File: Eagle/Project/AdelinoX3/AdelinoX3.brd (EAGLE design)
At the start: 47.5 x 53.3 mm, 102 parts, among them J1 DC-044-A, J2 YELLOW-8P-2.54, J3 YELLOW-6P-2.54, J4 YELLOW-8P-2.54, J5 YELLOW-8P-2.54, J6 4P-2.0, J7 YELLOW-2X3P-2.54, J8 4P-2.0, Q1 NCE3407A, Q2 CJ2305, SW1 TS-1101F, U1 CJT1117-3.3, U2 MP1496DJ-SOT23-8, U3 ESP-12F / OPL: 317060163 / SM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, U4 DNP, U5 ATMEGA32U4-MUR-QFN44, U6 DNP, X1 306010049_XTAL_16MHZ-3225_4P

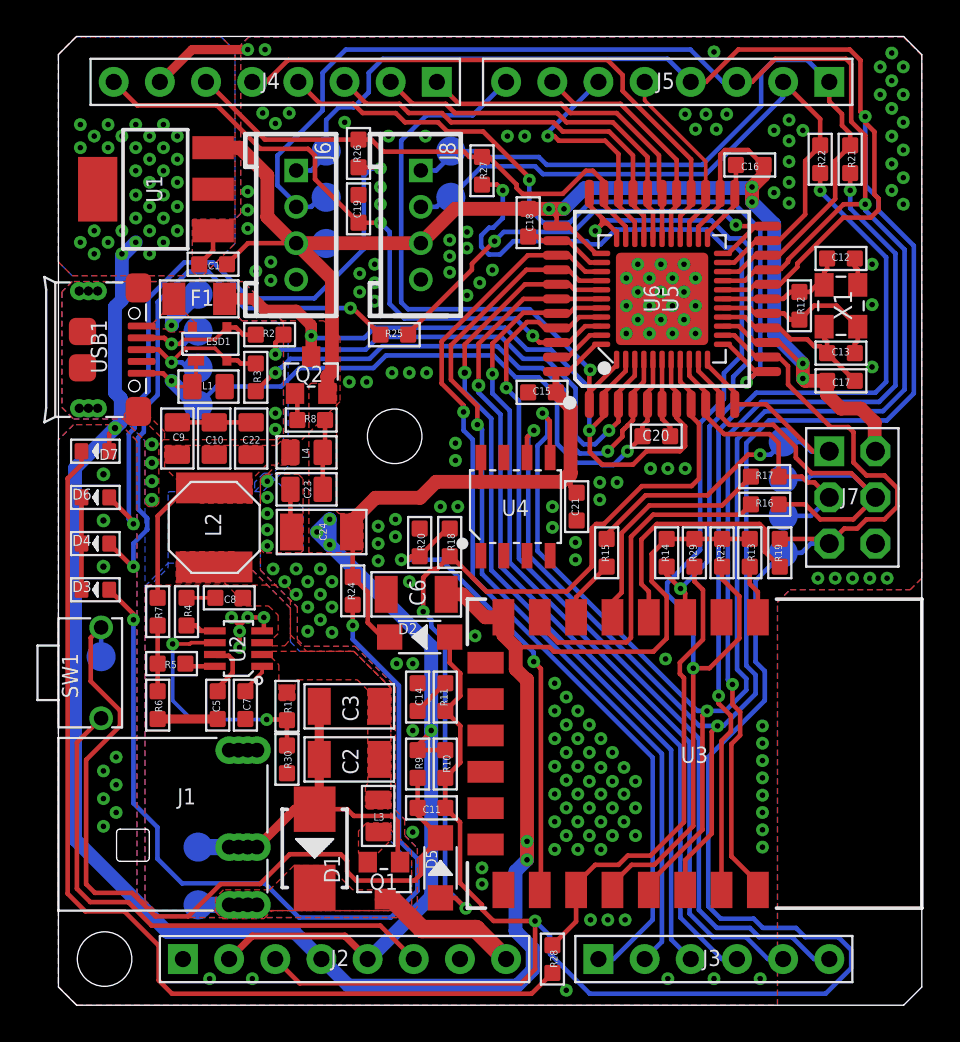
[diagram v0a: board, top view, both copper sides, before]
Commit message: Parts renumbered; tidy up silkscreen.
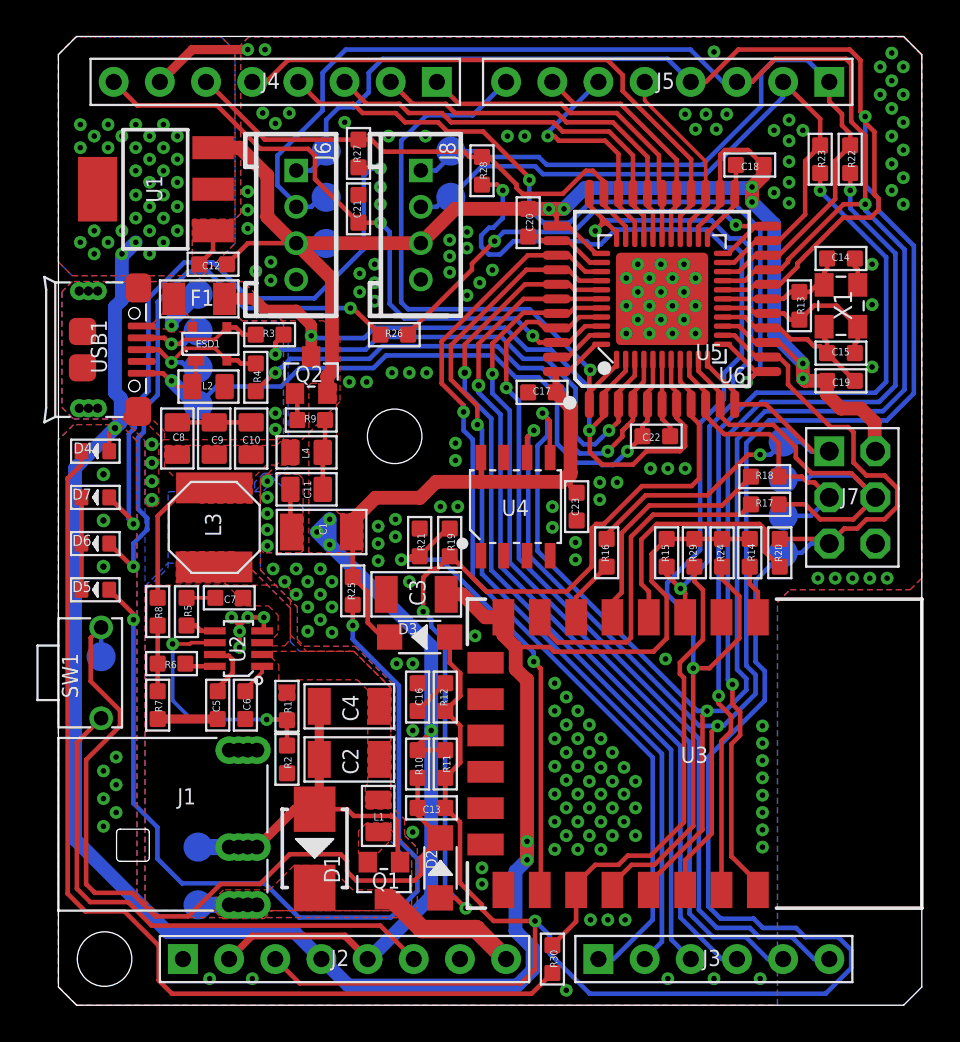
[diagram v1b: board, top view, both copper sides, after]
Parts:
- removed C24: 22uf, Seeed-Capacitor:C1206
- added C4: 22uf, Seeed-Capacitor:C1206
- C1: value 100nf -> 22uf; device OPL_Capacitor:C0603 -> Seeed-Capacitor:C1206
- C11, C8: value 100nf -> 10uf; device OPL_Capacitor:C0603 -> Seeed-Capacitor:C0805
- C12, C13: value 22pf -> 100nf; device Seeed-Capacitor:C0603 -> OPL_Capacitor:C0603
- C14, C15: value 100nf -> 22pf; device OPL_Capacitor:C0603 -> Seeed-Capacitor:C0603
- C20: value 1uf -> 100nf; device Seeed-Capacitor:C0603 -> OPL_Capacitor:C0603
- C21: device Seeed-Capacitor:C0603 -> OPL_Capacitor:C0603
- C22: value 10uf -> 1uf; device Seeed-Capacitor:C0805 -> Seeed-Capacitor:C0603
- C23: value 10uf -> 100nf; device Seeed-Capacitor:C0805 -> Seeed-Capacitor:C0603
- C3: device Seeed-Capacitor:C1206 -> OPL_Capacitor:C1206
- C6: value 22uf -> 22nf; device OPL_Capacitor:C1206 -> Seeed-Capacitor:C0603
- C7: value 22nf -> 100nf; device Seeed-Capacitor:C0603 -> OPL_Capacitor:C0603
- D3: value GRE-0603 -> 20V-500MA; device Seeed-LED:LED-0603 -> Seeed-Diode:SOD-123
- D4: value YEL-0603 -> BLU-0603
- D5: value 20V-500MA -> GRE-0603; device Seeed-Diode:SOD-123 -> Seeed-LED:LED-0603
- D7: value BLU-0603 -> YEL-0603
- L1: value 330R-1500MA -> 470R-2A; device Seeed-Inductor:L0805 -> OPL_Ferrite_and_Magnetic_Bead:L0805
- L2: value 10UH-225MA -> 330R-1500MA; device Seeed-Inductor:L5040S -> Seeed-Inductor:L0805
- L3: value 470R-2A -> 10UH-225MA; device OPL_Ferrite_and_Magnetic_Bead:L0805 -> Seeed-Inductor:L5040S
- R11: value 10K -> 100K
- R12: value 1M -> 10K
- R13: value 10K -> 1M
- R15, R24: value 1K -> 10K
- R19: value 0R -> 1K
- R2: value 22R -> 24K
- R20: value 100K -> 0R
- R21: value 1K -> 100K
- R23: value 10K -> 1K
- R28: value 470R -> 1K
- R30: value 24K -> 470R
- R4: value 10R -> 22R
- R5: value 3.3K -> 10R
- R6: value 3K / 1% -> 3.3K
- R7: value 2K7 / 1% -> 3K / 1%
- R8: value 100K -> 2K7 / 1%
- moved R28 43.5 mm to (23.3, 45.9), turned to 0 degrees
- moved C12 34.5 mm to (8.51, 40.8), turned to 90 degrees
- moved C16 34.5 mm to (19.8, 17.0), turned to 180 degrees
- moved C13 33.7 mm to (20.5, 10.9), turned to 270 degrees
- moved C14 33.5 mm to (43.1, 41.1), turned to 270 degrees
- moved R21 31.7 mm to (19.9, 25.5), turned to 0 degrees
- moved R12 29.0 mm to (21.3, 17.0)
- moved C19 28.2 mm to (43.1, 34.4), turned to 90 degrees
- moved L1 25.4 mm to (17.6, 10.4), turned to 90 degrees
- moved D5 24.4 mm to (2.03, 22.9), turned to 180 degrees
- moved R2 23.4 mm to (12.6, 13.5), turned to 180 degrees
- moved R23 22.3 mm to (41.9, 46.5)
- moved C22 22.3 mm to (32.9, 31.3), turned to 90 degrees
- moved R24 20.4 mm to (36.5, 24.9), turned to 180 degrees
- moved C21 20.3 mm to (16.5, 43.8), turned to 180 degrees
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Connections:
- net +3V3: now also C3.2, D4.+, R15.1, R24.2; no longer C6.2, D7.+, R13.1, R23.2
- net +5V: now also C11.2, C12.2, C19.1, C20.1, C23.1, D3.-, R10.1, R11.2, R25.1; no longer C15.1, C16.1, C21.1, C23.2, C24.2, D2.-, R10.2, R24.1, R8.1
- net ACT_LED: now also R26.1; no longer R25.1
- net AT_MISO: now also R16.1; no longer R15.1
- net AT_MOSI: now also R17.1; no longer R16.1
- net AT_SCK: now also R18.1; no longer R17.1
- net AT_SS: now also D2.+, R19.1; no longer D5.+, R18.1
- net BOOT_MODE: now also R24.1, R28.2; no longer R23.1, R27.2
- net D+: now also R4.2; no longer R3.2
- net D-: now also R3.2; no longer R2.2
- net ESP_EN: now also R15.2; no longer R14.2
- net GND: now also C11.1, C14.1, C15.1, C20.2, C23.2, C4.1, C8.1, D5.-, D7.-, L2.1, R2.1, R21.1, R7.1; no longer C13.1, C14.2, C15.2, C22.1, C23.1, C24.1, C7.1, D3.-, D4.-, L1.1, R20.1, R30.1, R6.1
- net GPIO12: now also R16.2; no longer R15.2
- net GPIO13: now also R17.2; no longer R16.2
- net GPIO14: now also R18.2; no longer R17.2
- net GPIO15: now also R19.2, R21.2; no longer R18.2, R20.2
- net GPIO16: now also R20.2; no longer R19.2
- net GPIO2_LED: now also R30.2; no longer R28.2
- net N$13: now also C16.1, R12.2; no longer C14.1, R11.2
- net N$15: now also C7.2, R5.2; no longer C8.2, R4.2
- net N$23: now also R7.2, R8.1; no longer R5.2, R7.1
- net N$3: now also R9.2; no longer R8.2
- net N$7: now also R2.2; no longer R30.2
- net N$8: now also L1.1; no longer L3.1
- net PIN_AREF: now also C21.1; no longer C19.1
- net PIN_D0: now also R22.2; no longer R21.2
- net PIN_D1: now also R23.2; no longer R22.2
- net PIN_D13: now also R28.1; no longer R26.1
- net RESET: now also C13.1, D3.+, R12.1, R20.1; no longer C11.1, D2.+, R10.1, R19.1
- net RST: now also R14.2; no longer R13.2
- net RSTAT: now also C13.2, D2.-, R10.2; no longer C11.2, D5.-, R9.2
- net RXD: now also R23.1; no longer R22.1
- net SW_BS: now also R5.1; no longer R4.1
- net SW_F1: now also C8.2, L3.2, R8.2; no longer C22.2, L2.2, R7.2
- net SW_FB: now also R6.1; no longer R5.1
- net SW_SS: now also C6.2; no longer C7.2
- net SW_VCC_IN: now also C4.2, L1.2; no longer C3.2, L3.2
- net SW_VCC_OUT: now also C7.1, L3.1; no longer C8.1, L2.1
- net TXD: now also R22.1; no longer R21.1
- net UCAP: now also C22.2; no longer C20.2
- net UD+: now also R4.1; no longer R3.1
- net UD-: now also R3.1; no longer R2.1
- net UGND: now also C22.1, L2.2; no longer C20.1, L1.2
- net XTAL1: now also C14.2, R13.2; no longer C12.2, R12.2
- net XTAL2: now also C15.2, R13.1; no longer C13.2, R12.1
- net _ACT: now also D6.+, R26.2; no longer D4.+, R25.2
- net _D13: now also D7.+, R27.2; no longer D6.+, R26.2
- net _ESP: now also D4.-, R30.1; no longer D7.-, R28.1
- net _PWR: now also D5.+, R25.2; no longer D3.+, R24.2
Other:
- board text added: "0"
- board text added: "33"
- board text added: "5"
- board text added: "6"
- board text added: "9"
- board text added: "F"
- board text added: "G"
- board text added: "N"
- board text added: "U"
- board text added: "V"
- board text added: "a"
- board text added: "e"
- board text added: "g"
- board text added: "i"
- board text added: "m"
- board text added: "n"
- board text added: "x"
- board text added: "~"
- board text removed: "-GND-"
- board text removed: "12"
- board text removed: "33V"
- board text removed: "AREF"
- board text removed: "ATmega32U4"
- board text removed: "R0"
- board text removed: "T1"
- board text removed: "Vin"
- board text removed: "~10"
- board text removed: "~11"
- board text removed: "~13"
- board text removed: "~3"
- board text removed: "~5"
- board text removed: "~6"
- board text removed: "~9"

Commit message: Add sensing pads; close vias; better test pad spacing.
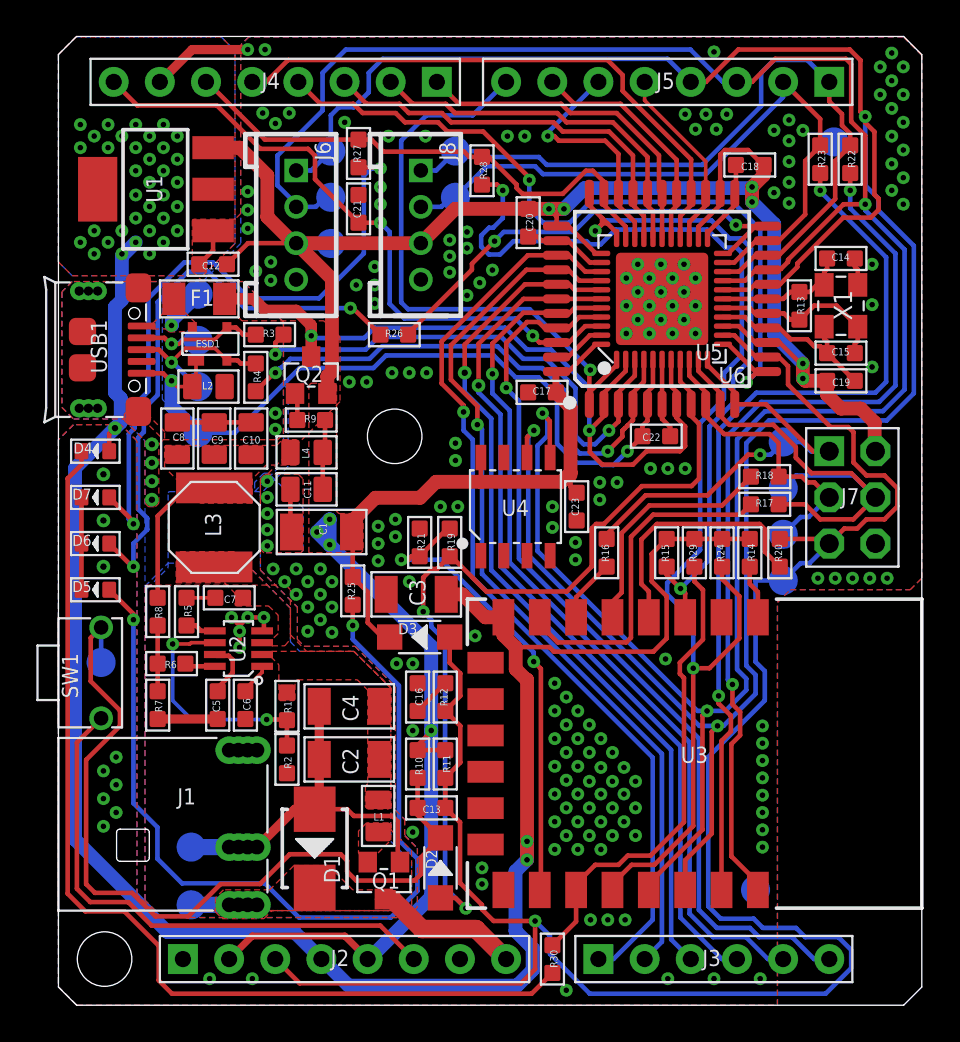
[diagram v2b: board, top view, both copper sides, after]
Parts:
- added TP18, TP19: TPTP16R, testpad:TP16R
- moved TP8 1.52 mm to (7.68, 31.5)
- moved TP3 1.52 mm to (39.9, 23.4)
- moved TP2 1.02 mm to (39.9, 25.9)
- moved TP7 1.02 mm to (7.68, 34.0)
- moved TP6 0.51 mm to (7.68, 36.6)
- moved TP4 0.51 mm to (39.9, 28.4)
- moved TP10 0.38 mm to (7.30, 8.70)
- moved TP9 0.38 mm to (7.30, 5.52)
- moved TP11 0.32 mm to (2.35, 18.9)
- moved TP12 0.25 mm to (21.8, 47.0)
- moved TP13 0.25 mm to (21.8, 44.5)
- moved TP14 0.25 mm to (15.0, 44.5)
- moved TP15 0.25 mm to (15.0, 47.0)
- moved TP17 0.25 mm to (15.0, 41.9)
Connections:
- net GND: now also TP18.TP, TP19.TP
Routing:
- net UGND: track 41.4 -> 43.4 mm
- net GND: track 99.4 -> 99.8 mm, vias 215 -> 214

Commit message: Change bitmaps resolution to be more compatible.
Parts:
- D4: value BLU-0603 -> BLUE-0603
- D5: value GRE-0603 -> GREEN-0603
- D6: value YEL-0603 -> YELLOW-0603
- U3: value ESP-12F / OPL: 317060163 / SMD WIFI Module -> ESP-12F / OPL: 317060163
